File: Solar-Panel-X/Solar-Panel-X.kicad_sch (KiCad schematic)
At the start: 55 parts, among them J1 FFC2B28-10-G, U1 TSL2561, U2 BQ25570RGRR

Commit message: Exported Gerbers
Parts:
- added H1, H2, H3, H4: MountingHole, MountingHole:MountingHole_2.2mm_M2_DIN965, symbol Mechanical:MountingHole
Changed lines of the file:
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@@
     (pin "2")
+  )
+  (symbol (lib_id "Mechanical:MountingHole") (at 197.739 119.253 0) (unit 1)
+    (in_bom yes) (on_board yes) (fields_autoplaced)
+    (property "Reference" "H1" (id 0) (at 200.279 118.4183 0)
+      (effects (font (size 1.27 1.27)) (justify left))
+    )
+    (property "Value" "MountingHole" (id 1) (at 200.279 120.9552 0)
+      (effects (font (size 1.27 1.27)) (justify left))
+    )
+    (property "Footprint" "MountingHole:MountingHole_2.2mm_M2_DIN965" (id 2) (at 197.739 119.253 0)
+      (effects (font (size 1.27 1.27)) hide)
+    )
+    (property "Datasheet" "~" (id 3) (at 197.739 119.253 0)
+      (effects (font (size 1.27 1.27)) hide)
+    )
+  )
+  (symbol (lib_id "Mechanical:MountingHole") (at 197.739 131.699 0) (unit 1)
+    (in_bom yes) (on_board yes) (fields_autoplaced)
+    (property "Reference" "H3" (id 0) (at 200.279 130.8643 0)
+      (effects (font (size 1.27 1.27)) (justify left))
+    )
+    (property "Value" "MountingHole" (id 1) (at 200.279 133.4012 0)
+      (effects (font (size 1.27 1.27)) (justify left))
+    )
+    (property "Footprint" "MountingHole:MountingHole_2.2mm_M2_DIN965" (id 2) (at 197.739 131.699 0)
+      (effects (font (size 1.27 1.27)) hide)
+    )
+    (property "Datasheet" "~" (id 3) (at 197.739 131.699 0)
+      (effects (font (size 1.27 1.27)) hide)
+    )
   )
   (symbol (lib_id "Connector_Generic:Conn_02x05_Odd_Even") (at 288.671 148.844 0) (unit 1)
@@
     (pin "9")
   )
+  (symbol (lib_id "Mechanical:MountingHole") (at 197.739 125.476 0) (unit 1)
+    (in_bom yes) (on_board yes) (fields_autoplaced)
+    (property "Reference" "H2" (id 0) (at 200.279 124.6413 0)
+      (effects (font (size 1.27 1.27)) (justify left))
+    )
+    (property "Value" "MountingHole" (id 1) (at 200.279 127.1782 0)
+      (effects (font (size 1.27 1.27)) (justify left))
+    )
+    (property "Footprint" "MountingHole:MountingHole_2.2mm_M2_DIN965" (id 2) (at 197.739 125.476 0)
+      (effects (font (size 1.27 1.27)) hide)
+    )
+    (property "Datasheet" "~" (id 3) (at 197.739 125.476 0)
+      (effects (font (size 1.27 1.27)) hide)
+    )
+  )
+  (symbol (lib_id "Mechanical:MountingHole") (at 197.866 138.049 0) (unit 1)
+    (in_bom yes) (on_board yes) (fields_autoplaced)
+    (property "Reference" "H4" (id 0) (at 200.406 137.2143 0)
+      (effects (font (size 1.27 1.27)) (justify left))
+    )
+    (property "Value" "MountingHole" (id 1) (at 200.406 139.7512 0)
+      (effects (font (size 1.27 1.27)) (justify left))
+    )
+    (property "Footprint" "MountingHole:MountingHole_2.2mm_M2_DIN965" (id 2) (at 197.866 138.049 0)
+      (effects (font (size 1.27 1.27)) hide)
+    )
+    (property "Datasheet" "~" (id 3) (at 197.866 138.049 0)
+      (effects (font (size 1.27 1.27)) hide)
+    )
+  )
   (sheet_instances
     (path "/" (page "1"))
@@
       (reference "D5") (unit 1) (value "SBDiode") (footprint "solarpanels:SB Diode")
     )
+    (path "/54cae88e-0c1e-4c17-9589-ea6ab2d12694"
+      (reference "H1") (unit 1) (value "MountingHole") (footprint "MountingHole:MountingHole_2.2mm_M2_DIN965")
+    )
+    (path "/af344df5-f8f1-4300-8c40-51d1681a9cb2"
+      (reference "H2") (unit 1) (value "MountingHole") (footprint "MountingHole:MountingHole_2.2mm_M2_DIN965")
+    )
+    (path "/60e57f7a-b7c2-462d-8ea4-3cfe65fa213f"
+      (reference "H3") (unit 1) (value "MountingHole") (footprint "MountingHole:MountingHole_2.2mm_M2_DIN965")
+    )
+    (path "/d0e74642-b451-4818-8635-6c6460d97fb7"
+      (reference "H4") (unit 1) (value "MountingHole") (footprint "MountingHole:MountingHole_2.2mm_M2_DIN965")
+    )
     (path "/812a4aef-276f-4b0a-9c8e-1e17ab0c35bd"

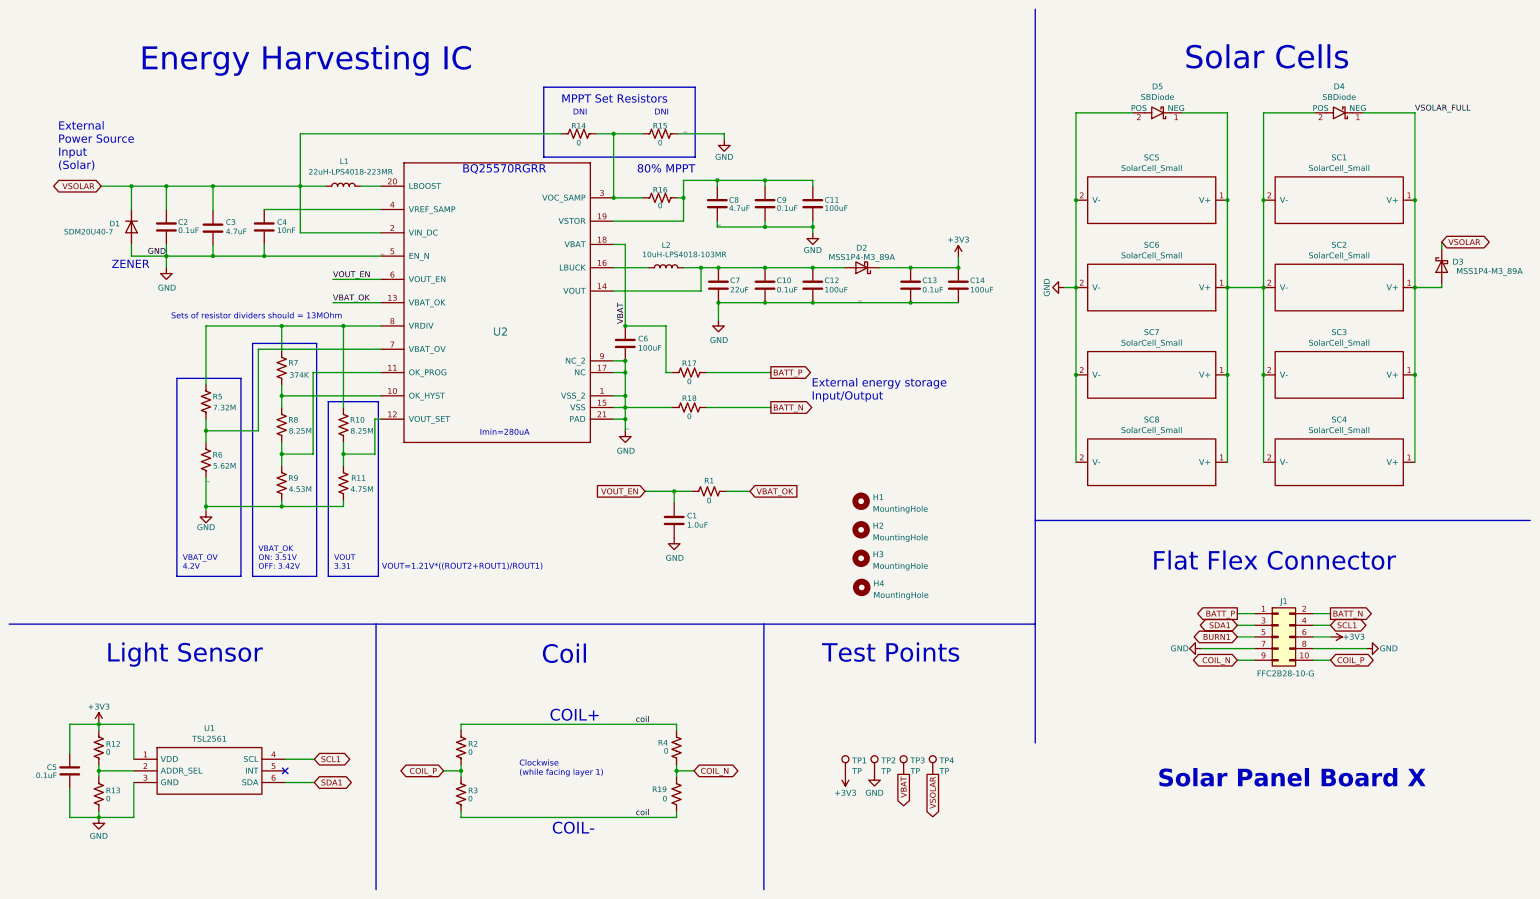
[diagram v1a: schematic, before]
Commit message: Stack architecture schematic updates / fixes
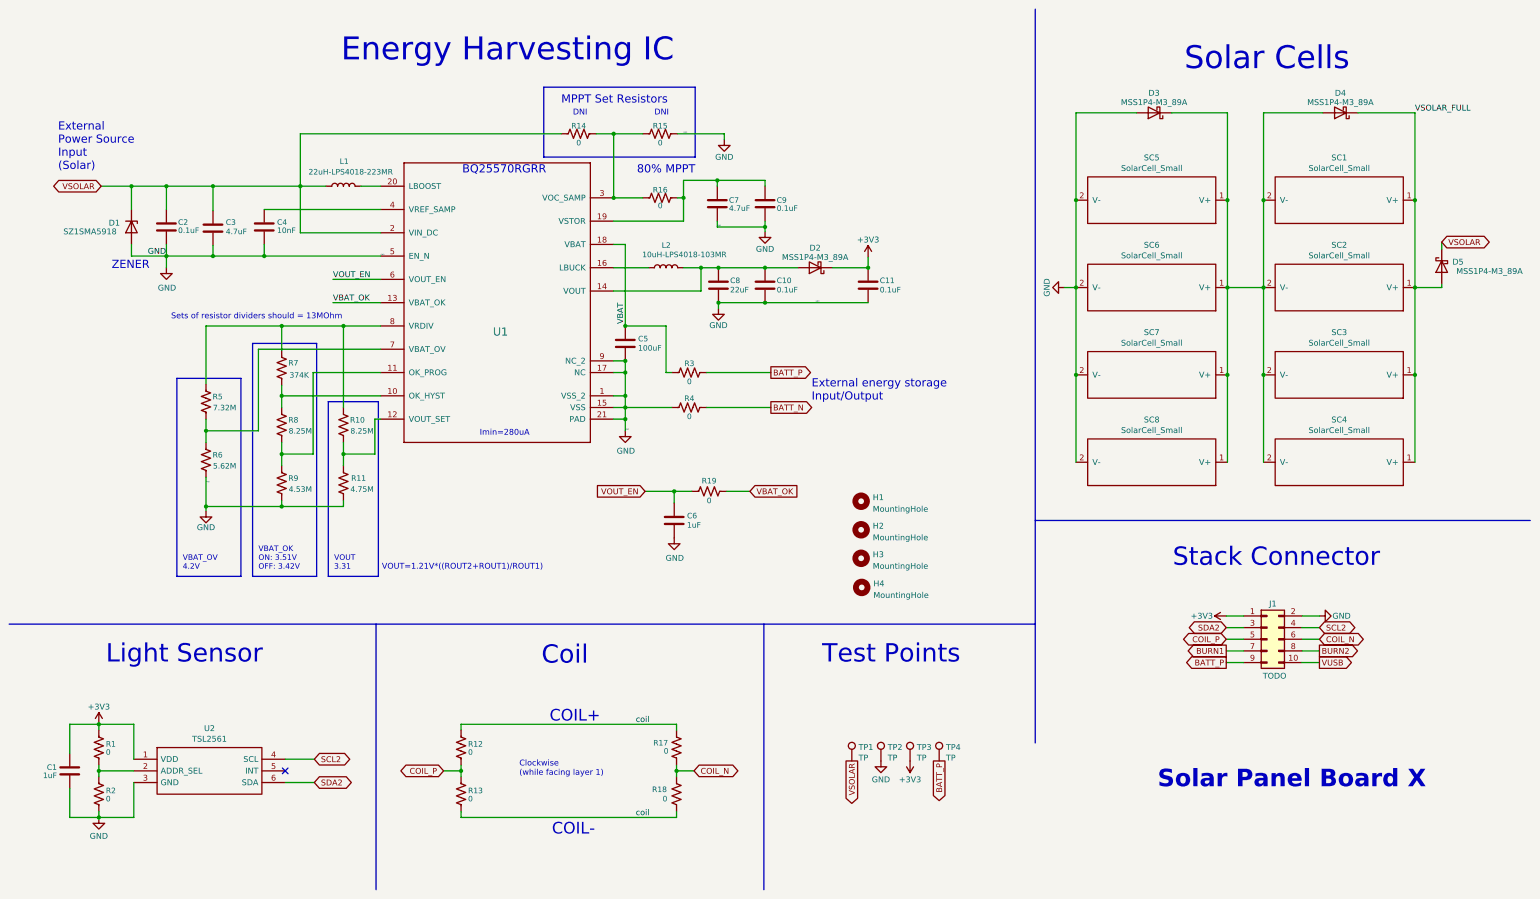
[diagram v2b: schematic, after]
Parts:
- removed C11, C12, C14: 100uF, Capacitor_SMD:C_0603_1608Metric, symbol Device:C
- removed D1: SDM20U40-7, Diode_SMD:D_SOD-523, symbol Device:D
- removed D4, D5: SBDiode, solarpanels:SB Diode, symbol solarpanels:SBDiode
- added D1: SZ1SMA5918, Diode_SMD:D_SMA, symbol Diode:Z1SMAxxx
- added D3, D4: MSS1P4-M3_89A, solarpanels:MICROSMP, symbol Device:D_Schottky
- C1: renamed from C5; value 0.1uF -> 1uF; footprint Capacitor_SMD:C_0402_1005Metric -> Capacitor_SMD:C_0603_1608Metric
- C10, C2, C3, C4, C9: footprint Capacitor_SMD:C_0402_1005Metric -> Capacitor_SMD:C_0603_1608Metric
- C11: renamed from C13; footprint Capacitor_SMD:C_0402_1005Metric -> Capacitor_SMD:C_0603_1608Metric
- C5: renamed from C6; footprint Capacitor_SMD:C_0402_1005Metric -> Capacitor_SMD:C_0805_2012Metric
- C6: renamed from C1; value 1.0uF -> 1uF; footprint Capacitor_SMD:C_0402_1005Metric -> Capacitor_SMD:C_0603_1608Metric
- C7: renamed from C8; footprint Capacitor_SMD:C_0402_1005Metric -> Capacitor_SMD:C_0603_1608Metric
- C8: renamed from C7; footprint Capacitor_SMD:C_0402_1005Metric -> Capacitor_SMD:C_0603_1608Metric
- J1: value FFC2B28-10-G -> TODO
- R1: renamed from R12; footprint Resistor_SMD:R_0402_1005Metric -> Resistor_SMD:R_0603_1608Metric
- R10, R11, R14, R15, R16, R5, R6, R7, R8, R9: footprint Resistor_SMD:R_0402_1005Metric -> Resistor_SMD:R_0603_1608Metric
- R12: renamed from R2; footprint Resistor_SMD:R_0402_1005Metric -> Resistor_SMD:R_0603_1608Metric
- R13: renamed from R3; footprint Resistor_SMD:R_0402_1005Metric -> Resistor_SMD:R_0603_1608Metric
- R17: renamed from R4; footprint Resistor_SMD:R_0402_1005Metric -> Resistor_SMD:R_0603_1608Metric
- R18: renamed from R19; footprint Resistor_SMD:R_0402_1005Metric -> Resistor_SMD:R_0603_1608Metric
- R19: renamed from R1; footprint Resistor_SMD:R_0402_1005Metric -> Resistor_SMD:R_0603_1608Metric
- R2: renamed from R13; footprint Resistor_SMD:R_0402_1005Metric -> Resistor_SMD:R_0603_1608Metric
- R3: renamed from R17; footprint Resistor_SMD:R_0402_1005Metric -> Resistor_SMD:R_0603_1608Metric
- R4: renamed from R18; footprint Resistor_SMD:R_0402_1005Metric -> Resistor_SMD:R_0603_1608Metric
- renumbered D3 to D5, U2 to U1, U1 to U2
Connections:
- net +3V3: now also J1.1 (Pin_1), TP3.1; no longer J1.6 (Pin_6), TP1.1
- net BATT_N: no longer J1.2 (Pin_2)
- net BATT_P: now also J1.9 (Pin_9), TP4.1; no longer J1.1 (Pin_1)
- net BURN1: now also J1.7 (Pin_7); no longer J1.5 (Pin_5)
- net COIL_N: now also J1.6 (Pin_6); no longer J1.9 (Pin_9)
- net COIL_P: now also J1.5 (Pin_5); no longer J1.10 (Pin_10)
- net GND: now also J1.2 (Pin_2), D1.2 (A), D3.2 (A); no longer J1.7 (Pin_7), J1.8 (Pin_8)
- net VBAT: no longer TP3.1
- net VSOLAR: now also TP1.1, D1.1 (K); no longer TP4.1
- net VSOLAR_FULL: now also D4.1 (K)
- net at SC1.2 (V-), SC2.2 (V-), SC3.2 (V-)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: now also D3.1 (K), D4.2 (A)
- net SCL1 renamed SCL2
- net SDA1 renamed SDA2
- new net BURN2: J1.8 (Pin_8)
- new net VUSB: J1.10 (Pin_10)
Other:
- note added: "Stack Connector"
- note removed: "Flat Flex Connector"
- moved on the sheet: C11, D2, TP1, TP2, TP3, TP4

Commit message: X board updates
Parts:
- added C12, C13: 10nF, Capacitor_SMD:C_0402_1005Metric, symbol Device:C
- added Q1, Q3: BSS138DWQ-7, Package_TO_SOT_SMD:SOT-363_SC-70-6, symbol mainboard:BSS138DWQ-7
- added Q2, Q4: MBT2222ADW1T1, Package_TO_SOT_SMD:SOT-363_SC-70-6, symbol Transistor_BJT:MBT2222ADW1T1
- added R20, R27: 680, Resistor_SMD:R_0402_1005Metric, symbol Device:R_US
- added R21, R28: 100K, Resistor_SMD:R_0402_1005Metric, symbol Device:R_US
- added R22, R23: 0, Resistor_SMD:R_0402_1005Metric, symbol Device:R_US
- added R24, R25, R29, R30: 10K, Resistor_SMD:R_0402_1005Metric, symbol Device:R_US
- added R26, R31: 200K, Resistor_SMD:R_0402_1005Metric, symbol Device:R_US
- C1, C10, C11, C2, C3, C4, C6, C7, C8, C9: footprint Capacitor_SMD:C_0603_1608Metric -> Capacitor_SMD:C_0402_1005Metric
- D1: value SZ1SMA5918 -> SZMM5Z5V1T1G; footprint Diode_SMD:D_SMA -> Diode_SMD:D_SOD-523
- J1: footprint solarpanels:GCT_FFC2B28-10-G -> Connector_PinHeader_1.27mm:PinHeader_2x05_P1.27mm_Vertical_SMD
- R1, R10, R11, R12, R13, R14, R15, R16, R17, R18, R19, R2, R3, R4, R5, R6, R7, R8, R9: footprint Resistor_SMD:R_0603_1608Metric -> Resistor_SMD:R_0402_1005Metric
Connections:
- net VUSB is gone; now on net GND: J1.10 (Pin_10)
- net +3V3: now also J1.9 (Pin_9), R21.1, R24.1, R25.1, R28.1, R29.1, R30.1; no longer J1.1 (Pin_1)
- net BATT_N: now also J1.2 (Pin_2)
- net BATT_P: now also J1.1 (Pin_1); no longer J1.9 (Pin_9), TP4.1
- net BURN1: now also J1.3 (Pin_3); no longer J1.7 (Pin_7)
- net BURN2: now also J1.4 (Pin_4); no longer J1.8 (Pin_8)
- net GND: now also C12.2, C13.2, Q1.1 (S2), Q1.4 (S1), Q3.1 (S2), Q3.4 (S1); no longer J1.2 (Pin_2)
- net SCL2: now also J1.8 (Pin_8), Q2.1 (E1), Q2.3 (C2), R22.2; no longer J1.4 (Pin_4), U2.4 (SCL)
- net SDA2: now also J1.7 (Pin_7), Q4.1 (E1), Q4.3 (C2), R23.2; no longer J1.3 (Pin_3), U2.6 (SDA)
- net VBAT: now also TP4.1
- new net: Q1.6 (D1), Q2.5 (B2), R20.2, R24.2
- new net: Q2.2 (B1), R20.1
- new net: C12.1, Q1.5 (G1), R26.2
- new net: Q3.2 (G2), Q3.3 (D2), R28.2
- new net: Q3.6 (D1), Q4.5 (B2), R27.2, R29.2
- new net: Q1.2 (G2), Q1.3 (D2), R21.2
- new net: C13.1, Q3.5 (G1), R31.2
- new net: Q4.2 (B1), R27.1
- new net SCL_LS: Q2.4 (E2), Q2.6 (C1), R22.1, R25.2, R26.1, U2.4 (SCL)
- new net SDA_LS: Q4.4 (E2), Q4.6 (C1), R23.1, R30.2, R31.1, U2.6 (SDA)
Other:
- note added: "I2C Bus Protection - Motor3"

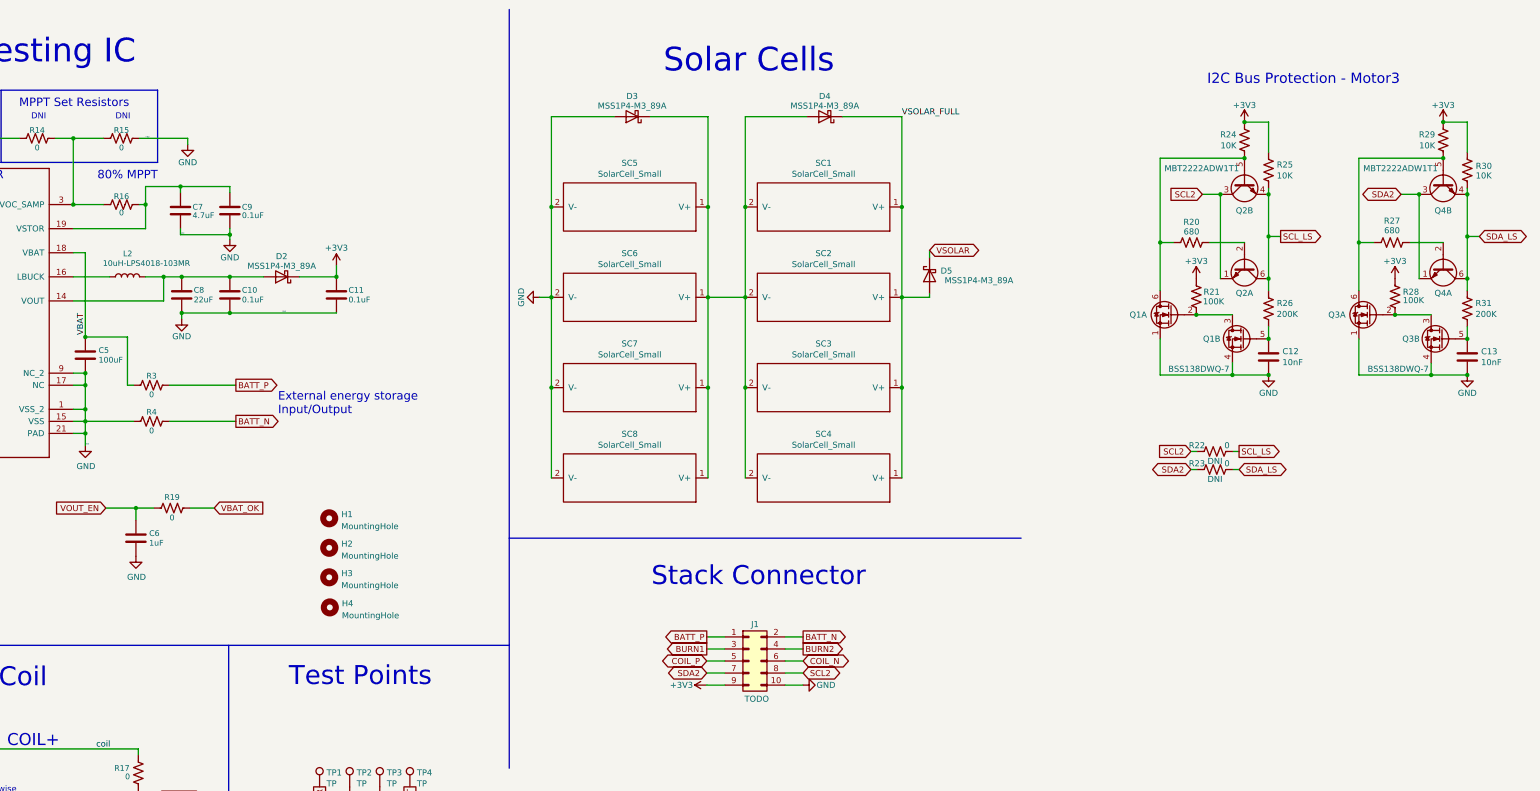
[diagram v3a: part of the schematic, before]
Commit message: X / Y+ board updates v04
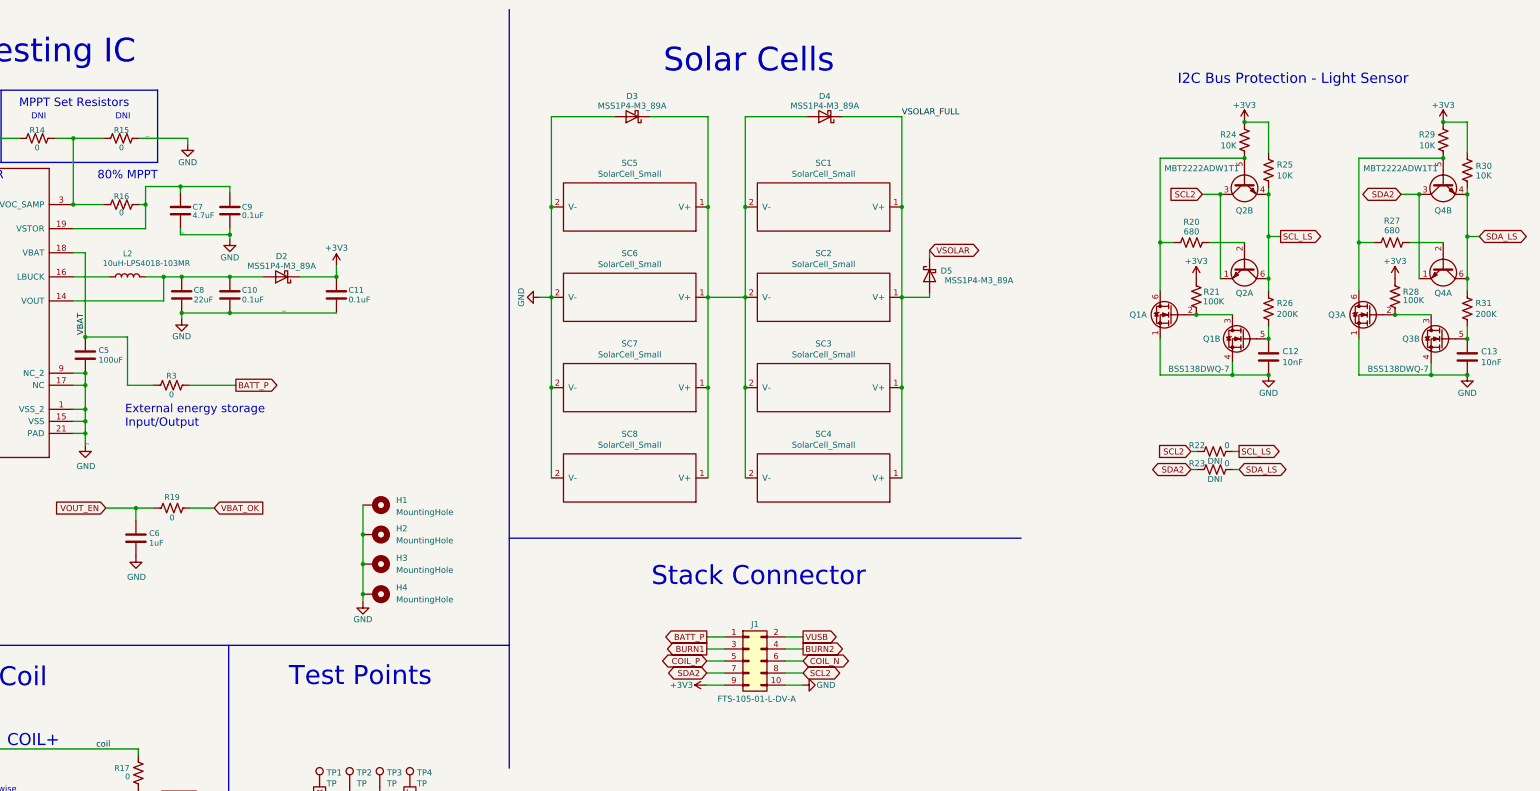
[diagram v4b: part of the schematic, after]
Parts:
- removed R4: 0, Resistor_SMD:R_0402_1005Metric, symbol Device:R_US
- H1, H2, H3, H4: footprint MountingHole:MountingHole_2.2mm_M2_DIN965 -> MountingHole:MountingHole_2.2mm_M2_DIN965_Pad; symbol Mechanical:MountingHole -> Mechanical:MountingHole_Pad
- J1: value TODO -> FTS-105-01-L-DV-A; footprint Connector_PinHeader_1.27mm:PinHeader_2x05_P1.27mm_Vertical_SMD -> batteryboard:FTS-105-XX-YY-DV-A
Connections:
- net GND: now also H1.1, H2.1, H3.1, H4.1
- net BATT_N renamed VUSB
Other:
- note added: "I2C Bus Protection - Light Sensor"
- note removed: "I2C Bus Protection - Motor3"
- moved on the sheet: R3
